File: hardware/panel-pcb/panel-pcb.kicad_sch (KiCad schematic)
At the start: 137 parts, among them J1 USB_C_Receptacle_USB2.0_16P, J10 RS-485 OUT, J11 12V_OUT, J2 SWD, J3 FSR North, J4 FSR East, J5 12V_IN, J6 FSR South, J7 FSR West, J8 RS-485 IN, J9 INT OUT, SW1 PANEL_ID, SW2 BOOTSEL, SW3 RS-485 Termination, U1 RP2040, U2 THVD1429, U3 W25Q32JV, U4 SN74AHCT125, U5 AMS1117-5.0, U6 AP7361C-33ER-13, U7 USBLC6-2SC6, U8 LM66200, X1 12MHz ABM8-272-T3

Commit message: Panel/master: AI-review metadata fixes + INT-path/latency docs
- ENIG surface finish on both boards (was unset)
- Panel C37/C44/C50/C52 value 25V->50V (match part C440198)
- Panel U2 datasheet URL -> THVD1429 (was THVD1420)
- Master D2-D10 TVS descriptions corrected to actual netlist wiring (sch+pcb)
- Master stackup note 'L3 power pours' -> 'L3 GND (solid)'
- Docs: SENSE_12V is a digital present-check; J9 pin2 -> dedicated GND;
  VUSB<->VIN bridge must stay intact; USB input-path authority + latency budget
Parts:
- C37, C44, C50, C52: value 10uF X5R 25V -> 10uF X5R 50V
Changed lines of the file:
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@@
 			)
 		)
-		(property "Value" "10uF X5R 25V"
+		(property "Value" "10uF X5R 50V"
 			(at 313.436 236.474 90)
 			(show_name no)
@@
 			)
 		)
-		(property "Value" "10uF X5R 25V"
+		(property "Value" "10uF X5R 50V"
 			(at 304.292 236.22 90)
 			(show_name no)
@@
 			)
 		)
-		(property "Datasheet" "https://www.ti.com/lit/ds/symlink/thvd1420.pdf"
+		(property "Datasheet" "https://www.ti.com/lit/ds/symlink/thvd1429.pdf"
 			(at 91.44 64.77 0)
 			(hide yes)
@@
 			)
 		)
-		(property "Value" "10uF X5R 25V"
+		(property "Value" "10uF X5R 50V"
 			(at 377.444 220.98 90)
 			(show_name no)
@@
 			)
 		)
-		(property "Value" "10uF X5R 25V"
+		(property "Value" "10uF X5R 50V"
 			(at 399.796 220.98 90)
 			(show_name no)

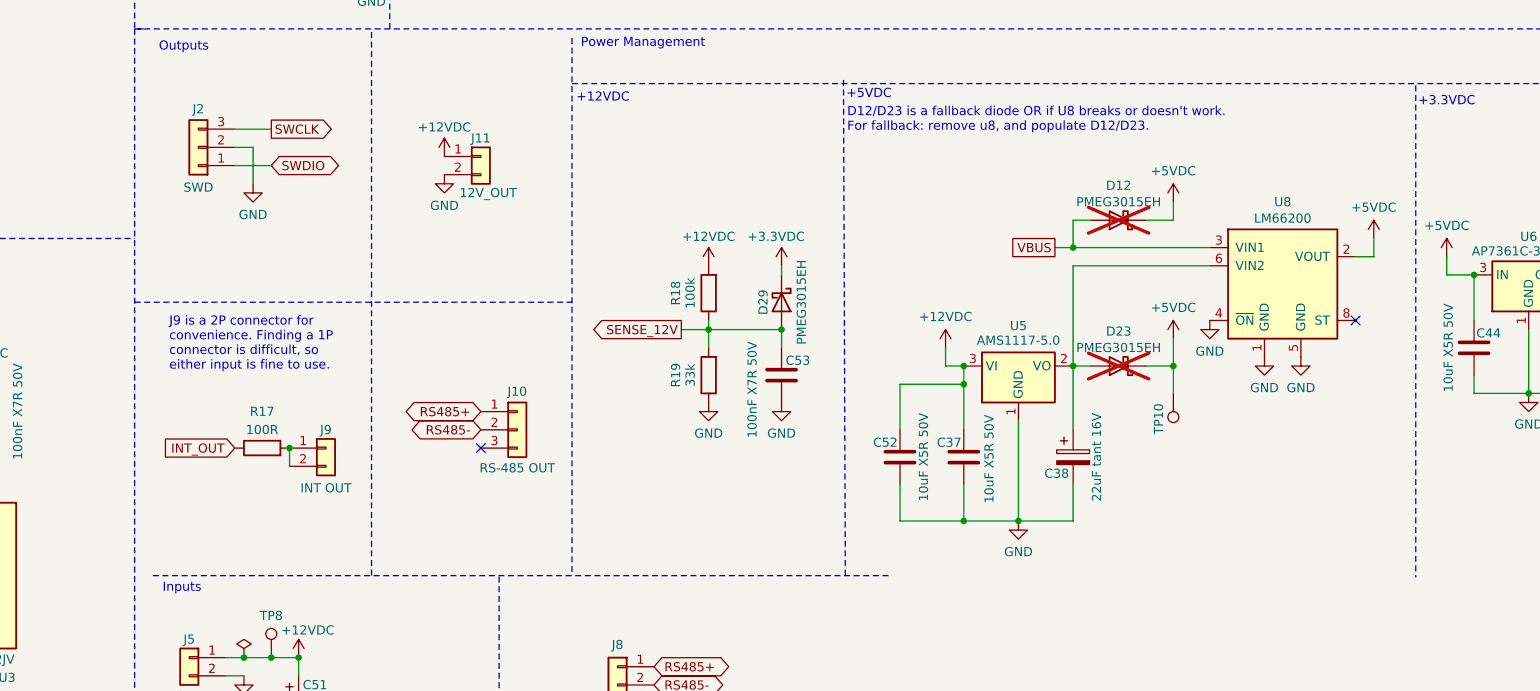
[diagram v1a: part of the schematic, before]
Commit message: Panel: post-review rework — INT TVS at J9, dedicated GND pin, U8 bypass caps
- D30 SMAJ5.0A ESD clamp at J9 (cathode->signal, anode->GND); R17 100R is the
  series element into the RP2040 (mirror of the master INT front-end)
- J9 pin 2 repurposed signal -> dedicated GND, pre-provisioning a paired
  signal+GND return cable (supersedes the both-pins-bridged arrangement)
- U8 (LM66200) local bypass added per review F4: C54 1uF (VBUS/VIN1),
  C56 1uF (AMS1117/VIN2), C55 100nF (VOUT/+5VDC)
- ERC/DRC clean. docs/PANEL_PCB.md updated. NOTE: D30 LCSC field still empty.
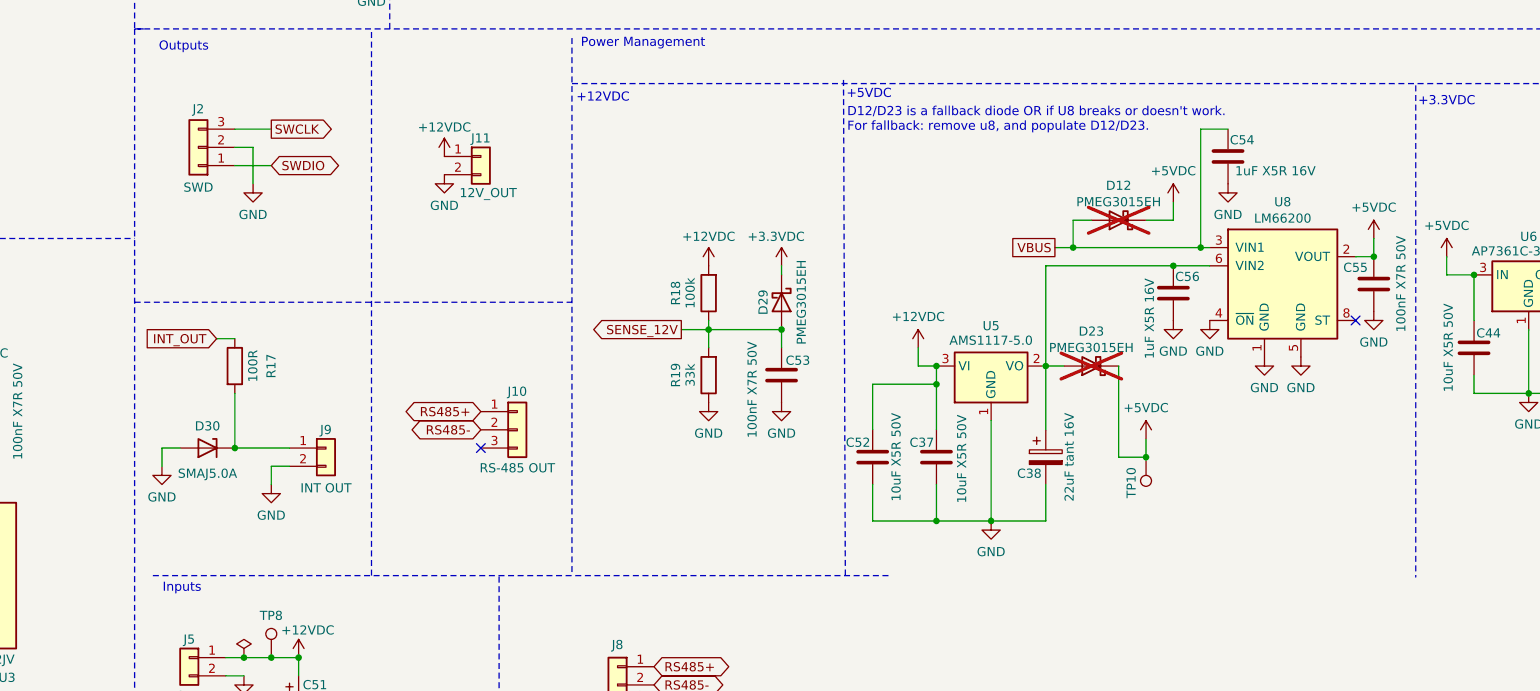
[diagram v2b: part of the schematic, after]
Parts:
- added C54, C56: 1uF X5R 16V, panel-pcb:C_0402_1005Metric_SilkTrim, symbol Device:C
- added C55: 100nF X7R 50V, panel-pcb:C_0402_1005Metric_SilkTrim, symbol Device:C
- added D30: SMAJ5.0A, Diode_SMD:D_SMA, symbol Device:D_Zener
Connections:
- net +5VDC: now also C55.1
- net GND: now also J9.2 (Pin_2), C54.1, C55.2, C56.1, D30.2 (A)
- net VBUS: now also C54.2
- net at J9.1 (Pin_1), R17.2: now also D30.1 (K); no longer J9.2 (Pin_2)
- net at C38.1, D23.2 (A), U5.2 (VO)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: now also C56.2
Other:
- note removed: "J9 is a 2P connector for convenience. Finding a 1P connector is difficult, so either input is fine to use."
- moved on the sheet: C37, C38, C52, D23, R17, TP10, U5

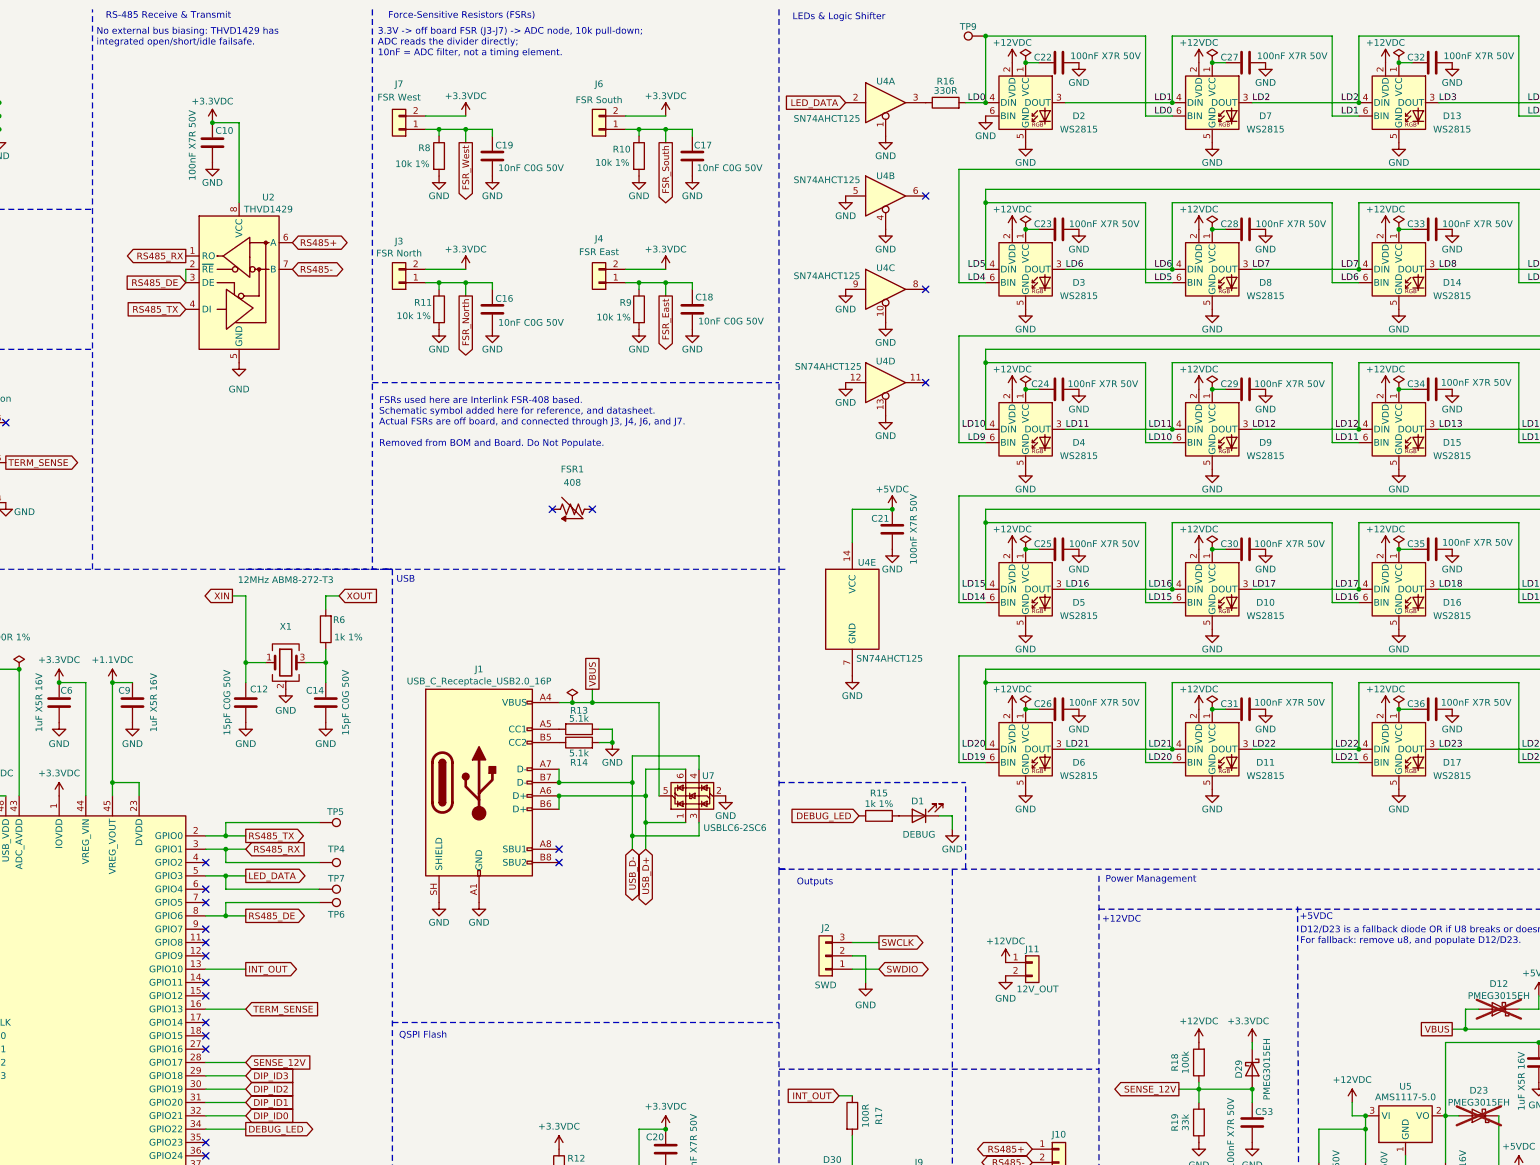
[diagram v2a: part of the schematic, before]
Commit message: Panel: diff-pair re-route for real stackup, QSPI meander fix, DRC honesty
The impedance geometry was calculated against KiCad's DEFAULT stackup
(3 x 0.48mm FR4) one day before the real JLC04161H-7628 stackup landed in
4594625. That put the reference plane at 0.2104mm instead of 0.48mm, so the
as-routed pairs were sitting near 55 ohm (USB) and 92 ohm (RS-485) against
90/120 targets. Impedance follows w/h, so a 2.28x thinner dielectric needs a
~2.1x narrower trace.

- USB re-routed to W=0.25/S=0.15 (~90 ohm), RS-485 to W=0.15/S=0.2 (~119
  ohm), both on F.Cu over the solid In1 GND plane. Netclass diff-pair widths
  updated to match.
- Both pairs length-matched: USB skew 0.023mm, RS-485 skew 0.019mm (via
  barrels counted at 1.5862mm each -- the legs carry different via counts
  because of the crossovers, so raw copper length understates the match).
- QSPI_SD3 tuning profile min_spacing 0.07 -> 0.15, closing review F6 (the
  meander's same-net gap was 0.09mm, JLC's absolute floor).
- Review F9 closed by correcting the rule rather than suppressing it: the
  .dru "pad to pad clearance (with hole, different nets)" rule relaxed 0.5 ->
  0.45mm, JLC's actual multilayer floor, which is exactly where J1's USB-C
  contacts sit. The generic "hole to hole clearance" rule stays at 0.5mm.
  The two are NOT interchangeable -- pad-to-pad is more specific and appears
  later, so it governs J1; relaxing only the generic rule brings all 14
  violations back.
- hole_to_hole, tuning_profile_track_geometries and missing_courtyard
  severities restored from "ignore" to enforced. Only the two library-naming
  rules remain ignored.
- AMS1117 output node labelled /+5VDC_AMS (was auto-net Net-(D23-A), named
  after a DNP diode). Zone display names now match their nets.
- TP13 (RS485+) / TP14 (RS485-) added. D30 sourced: LCSC C113952.

Verified with all remaining ignores lifted, --severity-all --schematic-parity
--refill-zones: 0 violations, 0 unconnected, ERC 0. Only cosmetic
footprint_filters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
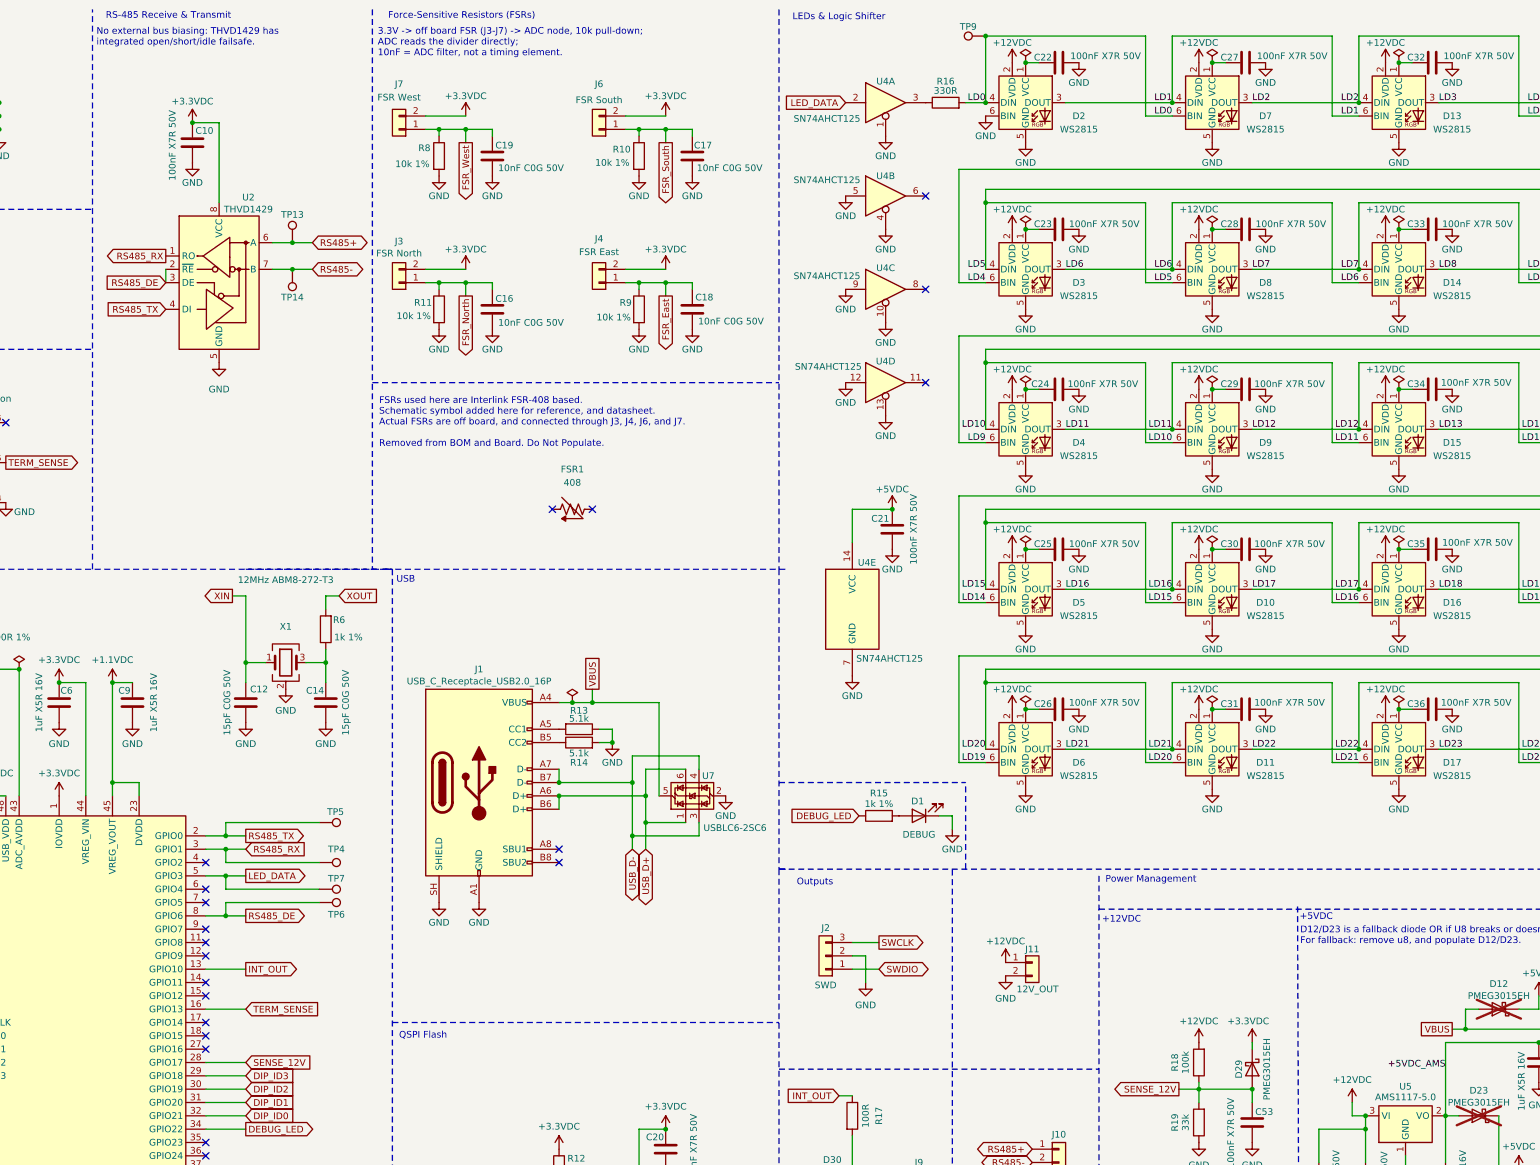
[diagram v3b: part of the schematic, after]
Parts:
- added TP13: RS485+, TestPoint:TestPoint_THTPad_D2.0mm_Drill1.0mm, symbol Connector:TestPoint
- added TP14: RS485-, TestPoint:TestPoint_THTPad_D2.0mm_Drill1.0mm, symbol Connector:TestPoint
- D30: LCSC (none) -> C113952
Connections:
- net RS485+: now also TP13.1
- net RS485-: now also TP14.1
- net +5VDC_AMS: now reaches C38.1, C56.2, D23.2 (A), U5.2 (VO), U8.6 (VIN2)
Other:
- moved on the sheet: C10, U2

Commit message: Panel: reassign SW3 + J1 footprints to the LCSC parts (schematic)
SW3  EG2201A -> panel-pcb:SW_SS22E01L5 (XKB SS22E01L5 DPDT, C609835)
J1   GCT USB4085 -> panel-pcb:USB_C_Receptacle_LCK_TCF829D_TEMPLATE (C53184807)

Changed at the schematic instance (source of truth); the library-cache
footprint is left alone. ERC still 0. On opening the PCB, "Update PCB from
Schematic" (F8) drops the new footprints in at the old anchors, re-nets their
pads by name (pins 1-6 for SW3; A1..B12+SH for J1 all match), and leaves the
old traces dangling for re-route.

The 4 confirm-parts (RN1 4610X, DIP-4 DS-04, DIP-3 DS-3P-BU, WJ500V terminal)
need NO change -- their existing footprints already accept the LCSC parts.
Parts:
- J1: footprint panel-pcb:USB_C_Receptacle_GCT_USB4085_EdgeTrim -> panel-pcb:USB_C_Receptacle_LCK_TCF829D_TEMPLATE
- SW3: footprint panel-pcb:SW_EG2201A -> panel-pcb:SW_SS22E01L5
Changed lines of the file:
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@@
 			)
 		)
-		(property "Footprint" "panel-pcb:USB_C_Receptacle_GCT_USB4085_EdgeTrim"
+		(property "Footprint" "panel-pcb:USB_C_Receptacle_LCK_TCF829D_TEMPLATE"
 			(at 137.16 160.02 0)
 			(hide yes)
@@
 			)
 		)
-		(property "Footprint" "panel-pcb:SW_EG2201A"
+		(property "Footprint" "panel-pcb:SW_SS22E01L5"
 			(at 73.914 98.806 0)
 			(hide yes)

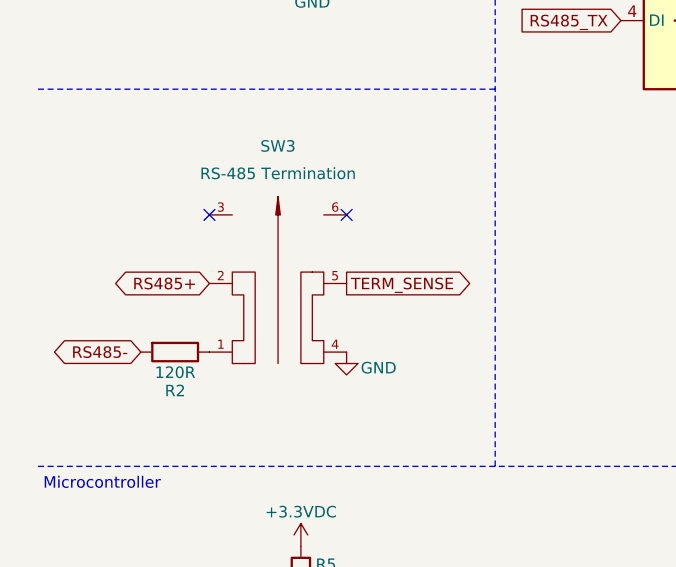
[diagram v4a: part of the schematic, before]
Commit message: Panel: LCSC part metadata, SW3 lugs as pads 7/8, stitching-via purge
PCB side of the SW3/J1 LCSC swap:
- J1 metadata USB4085-GF-A -> LCK-TCF829D + LCSC C53184807; SW3 EG2201A ->
  SS22E01L5, datasheet to the LCSC page, stale DigiKey fields dropped
  (sch + pcb). Closes the schematic-parity warning.
- J1's 9 starved_thermal errors fixed by making all 8 GND pads solid
  zone connections (library footprint + pcb instance). At 1mm pitch with a
  0.5mm thermal gap there is no room for a second spoke, and the shield
  posts' copper already merges with A12/B1.
- SW3 mounting lugs are pads 7 and 8 per the vendor/EasyEDA numbering
  (was MP1/MP2) and now have symbol pins, so they can be tied to GND.
  Symbol renamed EG2201A -> SS22E01L5 (lib, schematic cache and lib_id).
- 3D models: real SS22E01L5 from easyeda2kicad; J1 gets a clearly-labelled
  PLACEHOLDER model from a different USB-C part, for visual bulk only.

Via cleanup: the GND stitching vias had been generated ungrouped, so they
could not be batch-selected before re-routing. Classified every via by
whether it touches a track endpoint or pad -- 1089 were pour-only (36 of
them NOT flagged free, so that flag was the wrong filter). Removing all of
them leaves 0 unconnected items, proving none carried a routed connection,
but starves 26 GND pour islands. Deleted the 1034 pure stitching vias and
kept the 55 that are the sole feed for an island: 1332 -> 298 vias, zones
refilled, DRC 0 and no isolated copper.

Remaining by design: 2 ERC / 2 parity items for SW3 pins 7/8 awaiting
their GND wires in the schematic.
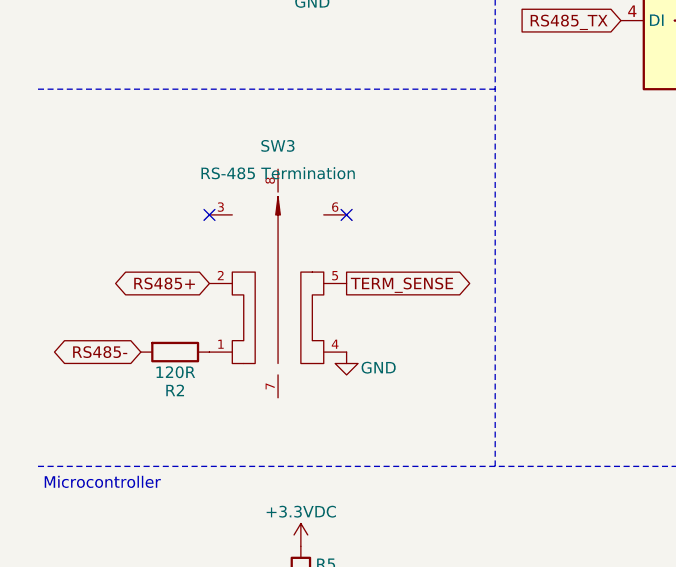
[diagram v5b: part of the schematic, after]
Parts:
- J1: DigiKey 2073-USB4085-GF-ACT-ND -> (none); LCSC (none) -> C53184807; MPN USB4085-GF-A -> LCK-TCF829D
- SW3: symbol panel-pcb:EG2201A -> panel-pcb:SS22E01L5; DigiKey EG1905-ND -> (none); LCSC (none) -> C609835; MPN EG2201A -> SS22E01L5
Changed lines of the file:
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@@
 			)
 		)
-		(property "MPN" "USB4085-GF-A"
+		(property "MPN" "LCK-TCF829D"
 			(at 137.16 160.02 0)
 			(hide yes)
@@
 			)
 		)
-		(property "DigiKey" "2073-USB4085-GF-ACT-ND"
+		(property "LCSC" "C53184807"
 			(at 0 0 0)
 			(hide yes)
@@
 	)
 	(symbol
-		(lib_id "panel-pcb:EG2201A")
+		(lib_id "panel-pcb:SS22E01L5")
 		(at 39.37 99.06 90)
 		(unit 1)
@@
 			)
 		)
-		(property "Datasheet" "https://www.digikey.com/en/products/detail/e-switch/EG2201A/101732"
+		(property "Datasheet" "https://www.lcsc.com/product-detail/C609835.html"
 			(at 70.866 99.06 0)
 			(hide yes)
@@
 			)
 		)
-		(property "MPN" "EG2201A"
+		(property "MPN" "SS22E01L5"
 			(at 23.622 99.06 0)
 			(hide yes)
@@
 			)
 		)
-		(property "DigiKey" "EG1905-ND"
+		(property "LCSC" "C609835"
 			(at 0 0 0)
 			(hide yes)
@@
 		(pin "6"
 		)
-		(instances
+		(pin "7"
+		)
+		(pin "8"
+		)
+		(instances
